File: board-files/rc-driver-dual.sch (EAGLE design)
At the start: 1 part

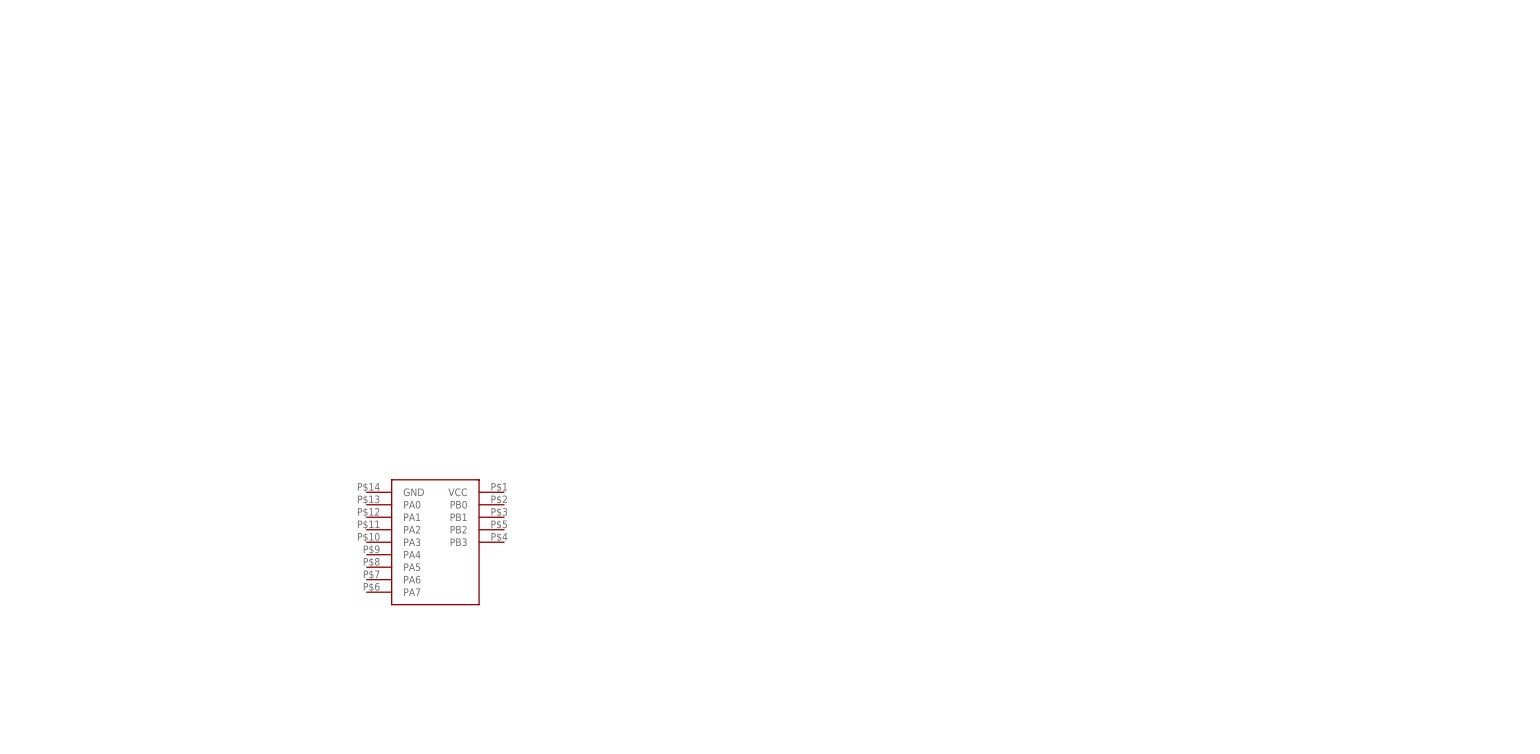
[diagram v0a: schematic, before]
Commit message: Added motor driver to dual driver board.
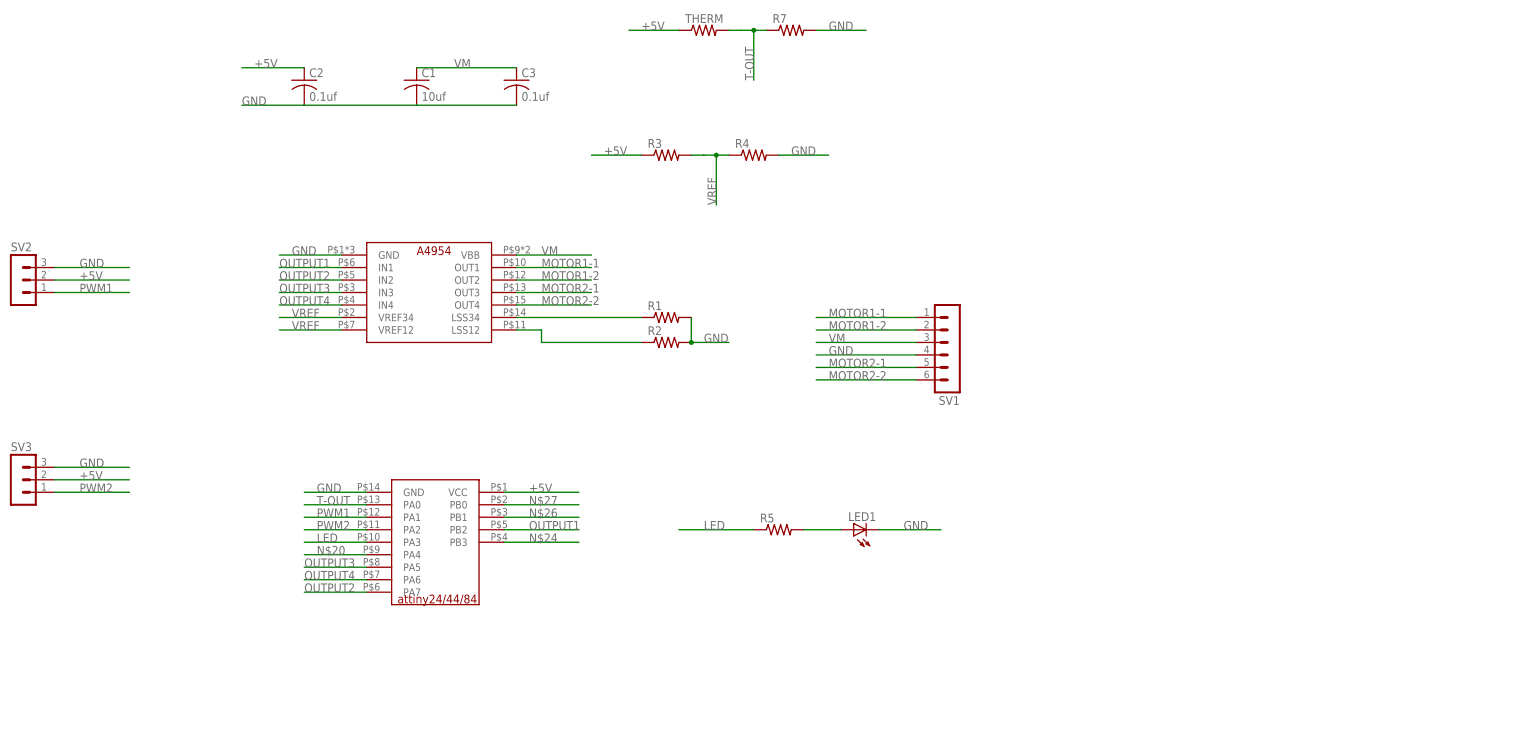
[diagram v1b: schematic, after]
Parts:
- added C1: 10uf, resistor:C-USC1206
- added C2, C3: 0.1uf, resistor:C-USC0603
- added LED1: (no value), led:LEDCHIPLED_0603
- added R1, R2: (no value), resistor:R-US_R0805W
- added R3, R4, R5, R7, THERM: (no value), resistor:R-US_R0603
- added SV1: (no value), con-lstb:MA06-1
- added SV2, SV3: (no value), con-lstb:MA03-1
- added U$2: A4954-DUAL-HBRIDGE, rc-parts:A4954-DUAL-HBRIDGE
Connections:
- new net +5V: C2.1, R3.1, SV2.2, SV3.2, THERM.1, U$1.VCC
- new net GND: C1.2, C2.2, C3.2, LED1.C, R1.2, R2.2, R4.2, R7.2, SV1.4, SV2.3, SV3.3, U$1.GND, U$2.GND
- new net LED: R5.1, U$1.PA3
- new net MOTOR1-1: SV1.1, U$2.OUT1
- new net MOTOR1-2: SV1.2, U$2.OUT2
- new net MOTOR2-1: SV1.5, U$2.OUT3
- new net MOTOR2-2: SV1.6, U$2.OUT4
- new net N$1: R1.1, U$2.LSS34
- new net N$2: R2.1, U$2.LSS12
- new net N$20: U$1.PA4
- new net N$24: U$1.PB3
- new net N$26: U$1.PB1
- new net N$27: U$1.PB0
- new net N$4: LED1.A, R5.2
- new net OUTPUT1: U$1.PB2, U$2.IN1
- new net OUTPUT2: U$1.PA7, U$2.IN2
- new net OUTPUT3: U$1.PA5, U$2.IN3
- new net OUTPUT4: U$1.PA6, U$2.IN4
- new net PWM1: SV2.1, U$1.PA1
- new net PWM2: SV3.1, U$1.PA2
- new net T-OUT: R7.1, THERM.2, U$1.PA0
- new net VM: C1.1, C3.1, SV1.3, U$2.VBB
- new net VREF: R3.2, R4.1, U$2.VREF12, U$2.VREF34

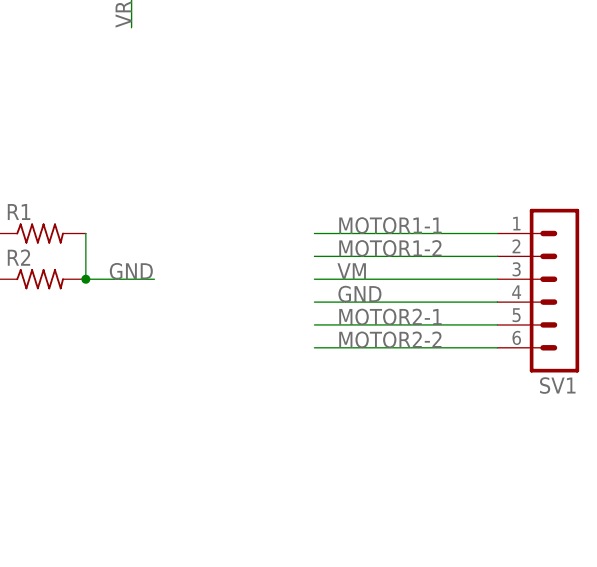
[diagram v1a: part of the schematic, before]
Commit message: fixing attiny silk. Shortened single rc-driver board.
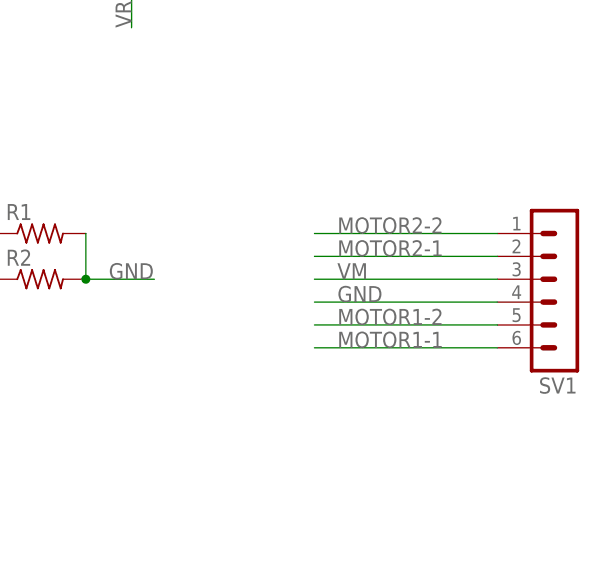
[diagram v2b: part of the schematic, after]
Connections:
- net MOTOR1-1: now also SV1.6; no longer SV1.1
- net MOTOR1-2: now also SV1.5; no longer SV1.2
- net MOTOR2-1: now also SV1.2; no longer SV1.5
- net MOTOR2-2: now also SV1.1; no longer SV1.6
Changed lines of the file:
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@@
 <?xml version="1.0" encoding="utf-8"?>
 <!DOCTYPE eagle SYSTEM "eagle.dtd">
-<eagle version="7.2.0">
+<eagle version="7.1.0">
 <drawing>
 <settings>
@@
 </segment>
 <segment>
-<pinref part="SV1" gate="1" pin="6"/>
-<wire x1="124.46" y1="55.88" x2="104.14" y2="55.88" width="0.1524" layer="91"/>
-<label x="106.68" y="55.88" size="1.778" layer="95"/>
+<pinref part="SV1" gate="1" pin="1"/>
+<wire x1="124.46" y1="68.58" x2="104.14" y2="68.58" width="0.1524" layer="91"/>
+<label x="106.68" y="68.58" size="1.778" layer="95"/>
 </segment>
 </net>
@@
 </segment>
 <segment>
-<pinref part="SV1" gate="1" pin="5"/>
-<wire x1="124.46" y1="58.42" x2="104.14" y2="58.42" width="0.1524" layer="91"/>
-<label x="106.68" y="58.42" size="1.778" layer="95"/>
+<pinref part="SV1" gate="1" pin="2"/>
+<wire x1="124.46" y1="66.04" x2="104.14" y2="66.04" width="0.1524" layer="91"/>
+<label x="106.68" y="66.04" size="1.778" layer="95"/>
 </segment>
 </net>
@@
 </segment>
 <segment>
-<pinref part="SV1" gate="1" pin="2"/>
-<wire x1="124.46" y1="66.04" x2="104.14" y2="66.04" width="0.1524" layer="91"/>
-<label x="106.68" y="66.04" size="1.778" layer="95"/>
+<pinref part="SV1" gate="1" pin="5"/>
+<wire x1="124.46" y1="58.42" x2="104.14" y2="58.42" width="0.1524" layer="91"/>
+<label x="106.68" y="58.42" size="1.778" layer="95"/>
 </segment>
 </net>
@@
 </segment>
 <segment>
-<pinref part="SV1" gate="1" pin="1"/>
-<wire x1="124.46" y1="68.58" x2="104.14" y2="68.58" width="0.1524" layer="91"/>
-<label x="106.68" y="68.58" size="1.778" layer="95"/>
+<pinref part="SV1" gate="1" pin="6"/>
+<wire x1="124.46" y1="55.88" x2="104.14" y2="55.88" width="0.1524" layer="91"/>
+<label x="106.68" y="55.88" size="1.778" layer="95"/>
 </segment>
 </net>

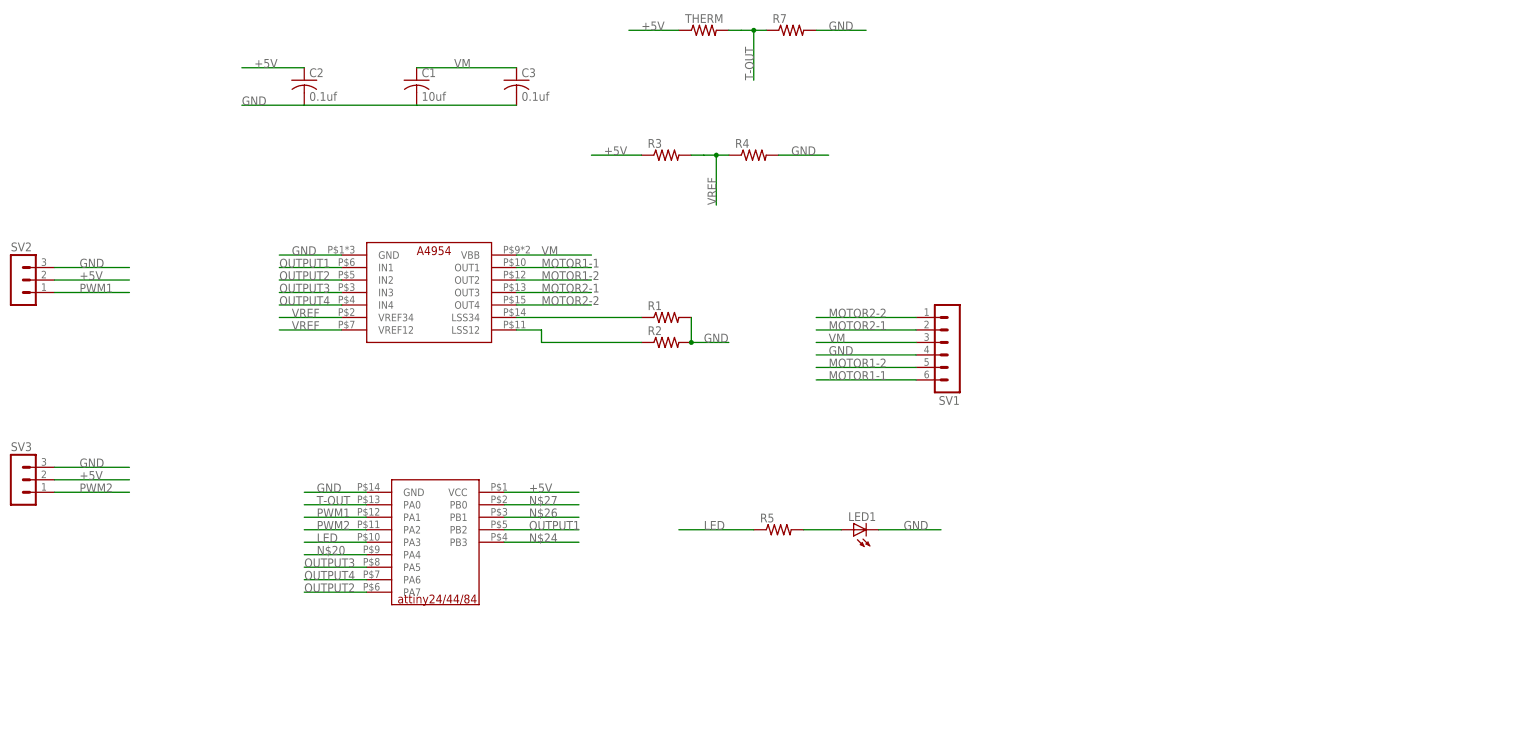
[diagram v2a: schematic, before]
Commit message: Added license to boards. Finished routingand silks.
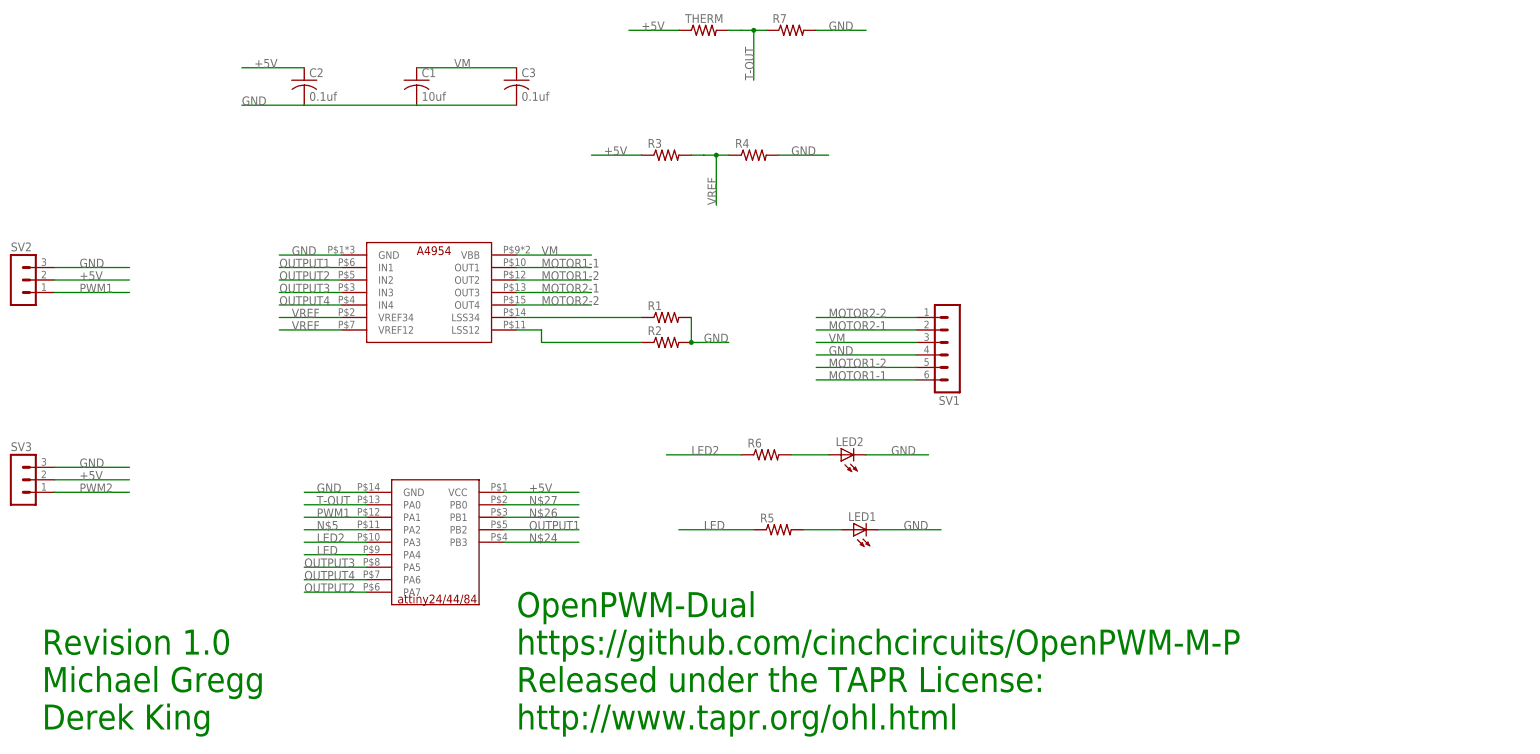
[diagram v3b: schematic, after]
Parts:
- added LED2: (no value), led:LEDCHIPLED_0603
- added R6: (no value), resistor:R-US_R0603
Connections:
- removed net N$20: U$1.PA4
- new net LED2: R6.1, U$1.PA3
- new net N$3: LED2.A, R6.2
- new net N$5: U$1.PA2
- net GND: now also LED2.C
- net LED: now also U$1.PA4; no longer U$1.PA3
- net PWM2: no longer U$1.PA2
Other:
- note added: "Derek King"
- note added: "Michael Gregg"
- note added: "OpenPWM-Dual"
- note added: "Released under the TAPR License:"
- note added: "Revision 1.0"
- note added: "http://www.tapr.org/ohl.html"
- note added: "https://github.com/cinchcircuits/OpenPWM-M-P"
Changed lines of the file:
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@@
 <?xml version="1.0" encoding="utf-8"?>
 <!DOCTYPE eagle SYSTEM "eagle.dtd">
-<eagle version="7.1.0">
+<eagle version="7.2.0">
 <drawing>
 <settings>
@@
 <part name="THERM" library="resistor" deviceset="R-US_" device="R0603"/>
 <part name="R7" library="resistor" deviceset="R-US_" device="R0603"/>
+<part name="R6" library="resistor" deviceset="R-US_" device="R0603"/>
+<part name="LED2" library="led" deviceset="LED" device="CHIPLED_0603"/>
 </parts>
 <sheets>
 <sheet>
 <plain>
+<text x="43.18" y="7.62" size="5.08" layer="91">OpenPWM-Dual</text>
+<text x="43.18" y="0" size="5.08" layer="91">https://github.com/cinchcircuits/OpenPWM-M-P</text>
+<text x="43.18" y="-7.62" size="5.08" layer="91">Released under the TAPR License:</text>
+<text x="43.18" y="-15.24" size="5.08" layer="91">http://www.tapr.org/ohl.html</text>
+<text x="-53.34" y="0" size="5.08" layer="91">Revision 1.0</text>
+<text x="-53.34" y="-7.62" size="5.08" layer="91">Michael Gregg</text>
+<text x="-53.34" y="-15.24" size="5.08" layer="91">Derek King</text>
 </plain>
 <instances>
@@
 <instance part="THERM" gate="G$1" x="81.28" y="127"/>
 <instance part="R7" gate="G$1" x="99.06" y="127"/>
+<instance part="R6" gate="G$1" x="93.98" y="40.64"/>
+<instance part="LED2" gate="G$1" x="109.22" y="40.64" rot="R90"/>
 </instances>
 <busses>
@@
 <label x="106.68" y="60.96" size="1.778" layer="95"/>
 </segment>
+<segment>
+<pinref part="LED2" gate="G$1" pin="C"/>
+<wire x1="114.3" y1="40.64" x2="127" y2="40.64" width="0.1524" layer="91"/>
+<label x="119.38" y="40.64" size="1.778" layer="95"/>
+</segment>
 </net>
 <net name="LED" class="0">
-<segment>
-<pinref part="U$1" gate="G$1" pin="PA3"/>
-<wire x1="12.7" y1="22.86" x2="0" y2="22.86" width="0.1524" layer="91"/>
-<label x="2.54" y="22.86" size="1.778" layer="95"/>
-</segment>
 <segment>
 <pinref part="R5" gate="G$1" pin="1"/>
@@
 <label x="81.28" y="25.4" size="1.778" layer="95"/>
 </segment>
-</net>
-<net name="N$20" class="0">
 <segment>
 <pinref part="U$1" gate="G$1" pin="PA4"/>
@@
 <wire x1="-50.8" y1="33.02" x2="-35.56" y2="33.02" width="0.1524" layer="91"/>
 <label x="-45.72" y="33.02" size="1.778" layer="95"/>
-</segment>
-<segment>
-<pinref part="U$1" gate="G$1" pin="PA2"/>
-<wire x1="12.7" y1="25.4" x2="0" y2="25.4" width="0.1524" layer="91"/>
-<label x="2.54" y="25.4" size="1.778" layer="95"/>
 </segment>
 </net>
@@
 </segment>
 </net>
+<net name="N$3" class="0">
+<segment>
+<pinref part="LED2" gate="G$1" pin="A"/>
+<pinref part="R6" gate="G$1" pin="2"/>
+<wire x1="106.68" y1="40.64" x2="99.06" y2="40.64" width="0.1524" layer="91"/>
+</segment>
+</net>
+<net name="LED2" class="0">
+<segment>
+<pinref part="R6" gate="G$1" pin="1"/>
+<wire x1="88.9" y1="40.64" x2="73.66" y2="40.64" width="0.1524" layer="91"/>
+<label x="78.74" y="40.64" size="1.778" layer="95"/>
+</segment>
+<segment>
+<pinref part="U$1" gate="G$1" pin="PA3"/>
+<wire x1="12.7" y1="22.86" x2="0" y2="22.86" width="0.1524" layer="91"/>
+<label x="2.54" y="22.86" size="1.778" layer="95"/>
+</segment>
+</net>
+<net name="N$5" class="0">
+<segment>
+<pinref part="U$1" gate="G$1" pin="PA2"/>
+<wire x1="12.7" y1="25.4" x2="0" y2="25.4" width="0.1524" layer="91"/>
+<label x="2.54" y="25.4" size="1.778" layer="95"/>
+</segment>
+</net>

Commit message: add drunken spriral
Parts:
- renumbered THERM to RT1
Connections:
- removed net N$24: U$1.PB3
- removed net N$26: U$1.PB1
- removed net N$27: U$1.PB0
- removed net N$5: U$1.PA2
- net PWM2: now also U$1.PA2
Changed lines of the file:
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@@
 <part name="R5" library="resistor" deviceset="R-US_" device="R0603"/>
 <part name="LED1" library="led" deviceset="LED" device="CHIPLED_0603"/>
-<part name="THERM" library="resistor" deviceset="R-US_" device="R0603"/>
+<part name="RT1" library="resistor" deviceset="R-US_" device="R0603"/>
 <part name="R7" library="resistor" deviceset="R-US_" device="R0603"/>
 <part name="R6" library="resistor" deviceset="R-US_" device="R0603"/>
@@
 <instance part="R5" gate="G$1" x="96.52" y="25.4"/>
 <instance part="LED1" gate="G$1" x="111.76" y="25.4" rot="R90"/>
-<instance part="THERM" gate="G$1" x="81.28" y="127"/>
+<instance part="RT1" gate="G$1" x="81.28" y="127"/>
 <instance part="R7" gate="G$1" x="99.06" y="127"/>
 <instance part="R6" gate="G$1" x="93.98" y="40.64"/>
@@
 <wire x1="22.86" y1="111.76" x2="0" y2="111.76" width="0.1524" layer="91"/>
 <label x="-12.7" y="111.76" size="1.778" layer="95"/>
+<junction x="22.86" y="111.76"/>
+<junction x="0" y="111.76"/>
 </segment>
 <segment>
@@
 </segment>
 </net>
-<net name="N$24" class="0">
-<segment>
-<pinref part="U$1" gate="G$1" pin="PB3"/>
-<wire x1="40.64" y1="22.86" x2="55.88" y2="22.86" width="0.1524" layer="91"/>
-<label x="45.72" y="22.86" size="1.778" layer="95"/>
-</segment>
-</net>
-<net name="N$26" class="0">
-<segment>
-<pinref part="U$1" gate="G$1" pin="PB1"/>
-<wire x1="40.64" y1="27.94" x2="55.88" y2="27.94" width="0.1524" layer="91"/>
-<label x="45.72" y="27.94" size="1.778" layer="95"/>
-</segment>
-</net>
-<net name="N$27" class="0">
-<segment>
-<pinref part="U$1" gate="G$1" pin="PB0"/>
-<wire x1="40.64" y1="30.48" x2="55.88" y2="30.48" width="0.1524" layer="91"/>
-<label x="45.72" y="30.48" size="1.778" layer="95"/>
-</segment>
-</net>
 <net name="+5V" class="0">
 <segment>
@@
 </segment>
 <segment>
-<pinref part="THERM" gate="G$1" pin="1"/>
+<pinref part="RT1" gate="G$1" pin="1"/>
 <wire x1="76.2" y1="127" x2="66.04" y2="127" width="0.1524" layer="91"/>
 <label x="68.58" y="127" size="1.778" layer="95"/>
@@
 <wire x1="-50.8" y1="33.02" x2="-35.56" y2="33.02" width="0.1524" layer="91"/>
 <label x="-45.72" y="33.02" size="1.778" layer="95"/>
+</segment>
+<segment>
+<pinref part="U$1" gate="G$1" pin="PA2"/>
+<wire x1="12.7" y1="25.4" x2="0" y2="25.4" width="0.1524" layer="91"/>
+<label x="2.54" y="25.4" size="1.778" layer="95"/>
 </segment>
 </net>
@@
 <segment>
 <pinref part="R7" gate="G$1" pin="1"/>
-<pinref part="THERM" gate="G$1" pin="2"/>
+<pinref part="RT1" gate="G$1" pin="2"/>
 <wire x1="93.98" y1="127" x2="91.44" y2="127" width="0.1524" layer="91"/>
 <wire x1="88.9" y1="127" x2="86.36" y2="127" width="0.1524" layer="91"/>
@@
 </segment>
 </net>
-<net name="N$5" class="0">
-<segment>
-<pinref part="U$1" gate="G$1" pin="PA2"/>
-<wire x1="12.7" y1="25.4" x2="0" y2="25.4" width="0.1524" layer="91"/>
-<label x="2.54" y="25.4" size="1.778" layer="95"/>
-</segment>
-</net>
 </nets>
 </sheet>
 </sheets>
+<errors>
+</errors>
 </schematic>
 </drawing>
